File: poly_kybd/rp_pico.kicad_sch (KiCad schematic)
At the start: 46 parts, among them SW2 EVQPUC02K, SW3 EVQPUC02K, U1 TLV62569DBVR, U10 RP2040, U11 TPD4E05U06DQAR, U9 W25Q64JVXGIQ, Y1 7M12000044

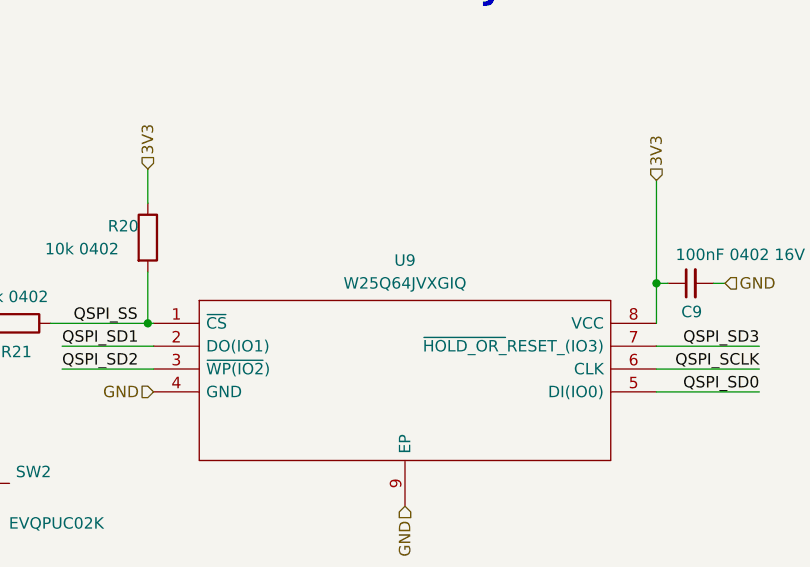
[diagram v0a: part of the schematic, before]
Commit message: A5: replace four EOL parts across schematics, PCBs and the project library
All four were discontinued at JLCPCB ("no longer manufactured", 0 stock),
so the v3.2 BOM can no longer be ordered as-is. Metadata only - every
replacement keeps the same footprint, so no layout or netlist changes.

  C118249  Sunlord  TC212A475K025Y  -> C5380411 Vishay  293D475X9025A2TE3
  C170128  Samsung  CL10C6R8DB8NNNC -> C318672  Samsung CL10C6R8CB8NNNC
  C3303719 Nexperia 74HC595BQ115    -> C730243  Nexperia 74HC595BQ,115
  C2940195 Winbond  W25Q64JVXGIQ    -> C5440778 Winbond W25Q64JVXGIM

Net cost at a 200-keyboard batch: -$4.15/keyboard, -$829/batch. The flash
carries it (-$4.76/kbd); the tantalum is the only real increase
(+$0.68/kbd, and it was the only 4.7uF/25V CASE-A with volume).

Also fixed along the way:

- MPN held the LCSC code rather than a manufacturer part number on all
  four, the same defect as the buffer in #24. Now the real MPN.
- The 74HC595 datasheet pointed at a rocelec.widen.net mirror that is now
  404. Repointed to Nexperia's own copy, verified to be the
  74HC595/74HCT595 data sheet. That URL was in poly_kb.kicad_sym too, so
  the project library and its cached copies are updated together.
- Manufacturer "winbond" -> "Winbond", "Sunlord" -> "Vishay".

Scope: the corne split42 variant shares these parts and is included -
leaving EOL codes anywhere is a trap. Library and footprint identifiers
containing "XGIQ" (lib_id, sym-lib-table path, footprint name, search
tags) are deliberately unchanged: they are names, not part numbers, and
renaming them would break the library binding.

Verified: 422 property edits across 14 files, insertions and deletions
exactly balanced, and every changed line is a (property ...) line - no
pads, nets, placements or reference designators touched.

Co-Authored-By: Claude Opus 5 <noreply@anthropic.com>
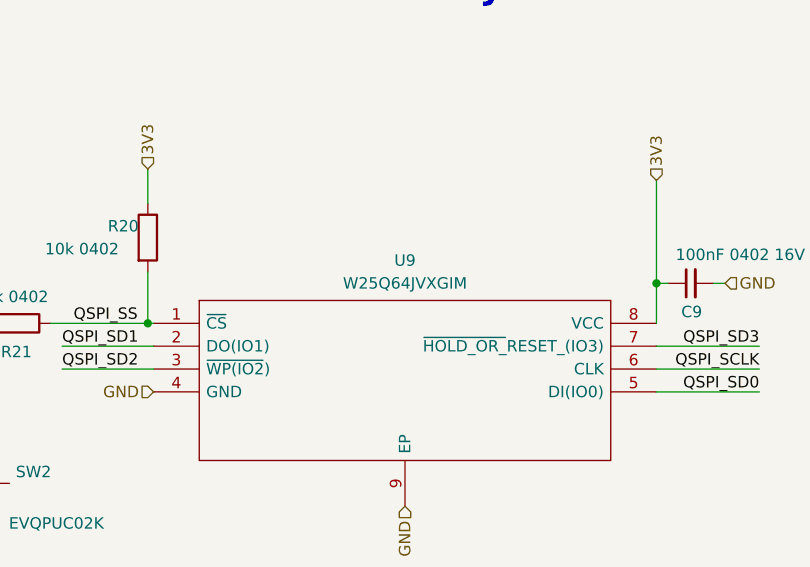
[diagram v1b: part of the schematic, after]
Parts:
- C5: JLC C170128 -> C318672; LCSC C170128 -> C318672; MPN C170128 -> CL10C6R8CB8NNNC
- U9: value W25Q64JVXGIQ -> W25Q64JVXGIM; JLC C2940195 -> C5440778; LCSC C2940195 -> C5440778; MPN C2940195 -> W25Q64JVXGIM; Manufacturer winbond -> Winbond
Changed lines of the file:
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@@
 			)
 		)
-		(property "Value" "W25Q64JVXGIQ"
+		(property "Value" "W25Q64JVXGIM"
 			(at 76.2 224.79 0)
 			(effects
@@
 			)
 		)
-		(property "Datasheet" "https://www.winbond.com/hq/search-resource-file.jsp?partNo=W25Q64JVXGIQ&type=datasheet"
+		(property "Datasheet" "https://www.winbond.com/resource-files/W25Q64JV%20RevK%2003102021%20Plus.pdf"
 			(at 100.33 229.235 0)
 			(effects
@@
 			)
 		)
-		(property "MPN" "C2940195"
+		(property "MPN" "W25Q64JVXGIM"
 			(at 100.33 231.775 0)
 			(effects
@@
 			)
 		)
-		(property "JLC" "C2940195"
+		(property "JLC" "C5440778"
 			(at 48.26 229.235 0)
 			(effects
@@
 			)
 		)
-		(property "LCSC" "C2940195"
+		(property "LCSC" "C5440778"
 			(at 48.26 229.235 0)
 			(effects
@@
 			)
 		)
-		(property "Manufacturer" "winbond"
+		(property "Manufacturer" "Winbond"
 			(at 48.26 229.235 0)
 			(effects
@@
 			)
 		)
-		(property "Datasheet" "https://www.lcsc.com/datasheet/lcsc_datasheet_2304140030_Samsung-Electro-Mechanics-CL10C6R8DB8NNNC_C170128.pdf"
+		(property "Datasheet" "https://wmsc.lcsc.com/wmsc/upload/file/pdf/v2/lcsc/2304140030_Samsung-Electro-Mechanics-CL10C6R8CB8NNNC_C318672.pdf"
 			(at 238.76 53.975 0)
 			(effects
@@
 			)
 		)
-		(property "MPN" "C170128"
+		(property "MPN" "CL10C6R8CB8NNNC"
 			(at 238.76 53.975 0)
 			(effects
@@
 			)
 		)
-		(property "JLC" "C170128"
+		(property "JLC" "C318672"
 			(at 238.76 53.975 0)
 			(effects
@@
 			)
 		)
-		(property "LCSC" "C170128"
+		(property "LCSC" "C318672"
 			(at 238.76 53.975 0)
 			(effects
